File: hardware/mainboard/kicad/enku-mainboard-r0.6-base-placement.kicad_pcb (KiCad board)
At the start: 4 copper layers, 59 x 101 mm, 120 parts, among them J1 1S LiPo + NTC, J2 Hirose DM3AT-SF-PEJM5, J3 FH34SRJ-24S-0.5SH(50), J5 GCT USB4105-GF-A-120, J6 4-pin pogo dock, J7 Tag-Connect TC2030-IDC-NL, Q1 IRLML6346TRPBF, SW1 HARD POWER, SW2 BOOT / RECOVERY, SW3 BTN_L1, SW4 BTN_L2, SW5 BTN_R1, SW6 BTN_R2, U1 ESP32-S3-WROOM-1-N16R8, U2 TPS2121, U3 BQ25185DLHR, U4 TPS63802DLAR, U5 BMI270, U8 USBLC6-2SC6

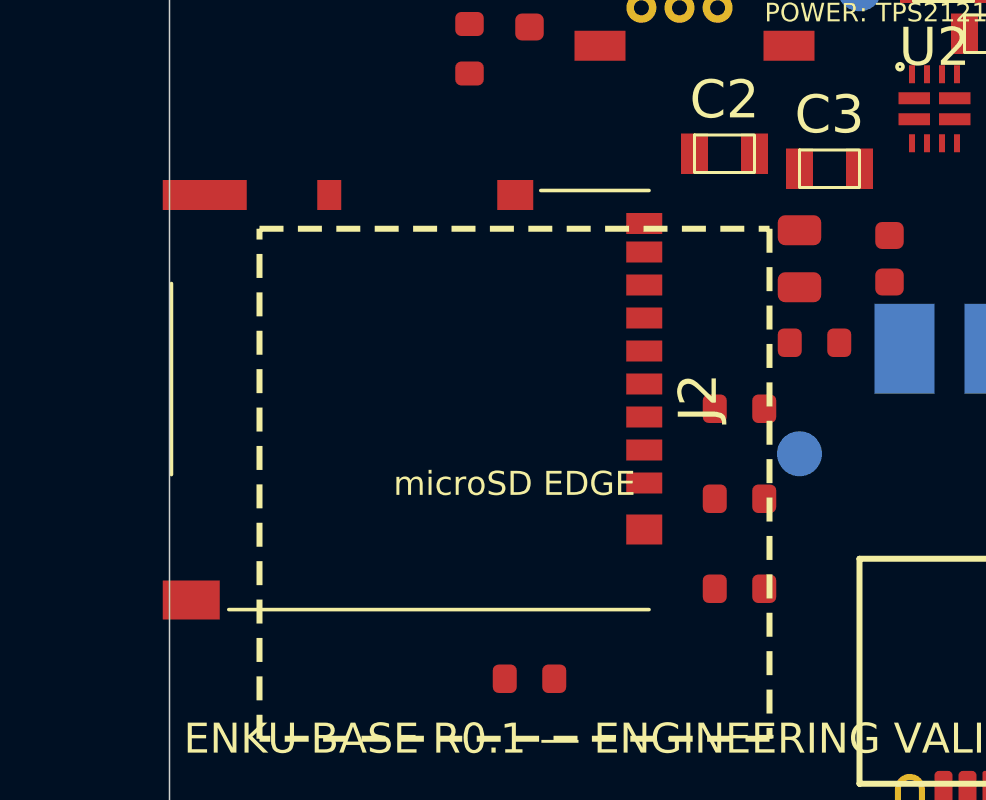
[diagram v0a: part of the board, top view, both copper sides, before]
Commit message: Correct Hirose J2 copper edge clearance by inward placement
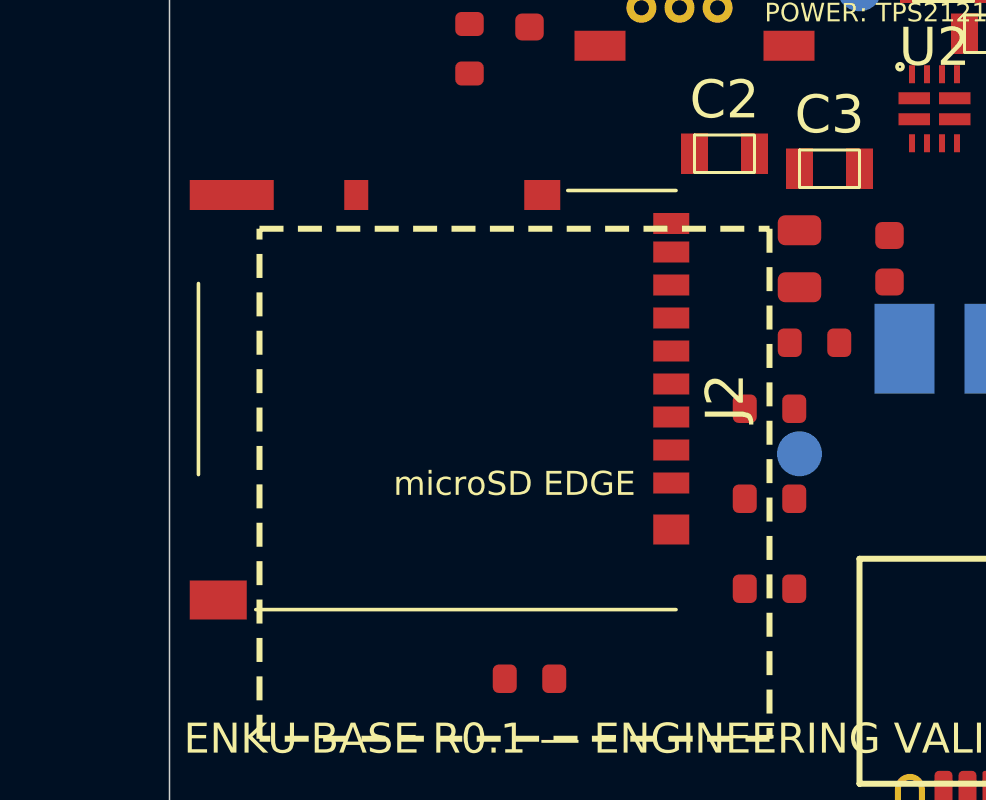
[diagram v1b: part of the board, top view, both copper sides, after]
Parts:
- moved R19 1.00 mm to (38.0, 101.0)
- moved R20 1.00 mm to (38.0, 104.0)
- moved R21 1.00 mm to (38.0, 107.0)
- moved J2 0.90 mm to (27.0, 100.7)
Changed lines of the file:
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@@
   )
   (footprint "ENKU:MICROSD_DM3AT_ENKU" (layer "F.Cu")
-    (at 26.1 100.7 270)
+    (at 27 100.7 270)
     (property "Reference" "J2" (at -0.075 -9.525 90) (layer "F.SilkS"))
     (property "Value" "Hirose DM3AT-SF-PEJM5" (at -0.075 9.575 90) (layer "F.Fab") hide)
@@
   )
   (footprint "Resistor_SMD:R_0603_1608Metric" (layer "F.Cu")
-    (at 37 101)
+    (at 38 101)
     (property "Reference" "R19" (at 0 -1.5 0) (layer "F.SilkS") hide)
     (property "Value" "0R" (at 0 1.5 0) (layer "F.Fab") hide)
@@
   )
   (footprint "Resistor_SMD:R_0603_1608Metric" (layer "F.Cu")
-    (at 37 107)
+    (at 38 107)
     (property "Reference" "R21" (at 0 -1.5 0) (layer "F.SilkS") hide)
     (property "Value" "0R (22R tune)" (at 0 1.5 0) (layer "F.Fab") hide)
@@
   )
   (footprint "Resistor_SMD:R_0603_1608Metric" (layer "F.Cu")
-    (at 37 104)
+    (at 38 104)
     (property "Reference" "R20" (at 0 -1.5 0) (layer "F.SilkS") hide)
     (property "Value" "0R (22R tune)" (at 0 1.5 0) (layer "F.Fab") hide)

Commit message: layout: move legacy study annotations off Base fabrication silkscreen and remove frontlight ghost zone
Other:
- board text removed: "FL REMAP 0R / DNP"
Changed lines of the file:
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@@
     (stroke (width 0.05) (type default)) (fill none) (layer "Edge.Cuts"))
   (gr_text "ENKU MAINBOARD R0.1 — PORTRAIT PCB SHELL"
-    (at 47 22.5) (layer "F.SilkS")
+    (at 47 22.5) (layer "Dwgs.User")
     (effects (font (size 1.2 1.2) (thickness 0.2))))
   (gr_text "ENKU BASE R0.1 — ENGINEERING VALIDATION"
-    (at 34.5 112.0) (layer "F.SilkS")
+    (at 34.5 112.0) (layer "Dwgs.User")
     (effects (font (size 1 1) (thickness 0.18))))
   (gr_rect (start 20.5 21) (end 26.25 69)
-    (stroke (width 0.2) (type dash)) (fill none) (layer "F.SilkS"))
+    (stroke (width 0.2) (type dash)) (fill none) (layer "Dwgs.User"))
   (gr_text "ESP32 ANTENNA KEEP-OUT"
-    (at 21.6 46.5 90) (layer "F.SilkS")
+    (at 21.6 46.5 90) (layer "Dwgs.User")
     (effects (font (size 0.8 0.8) (thickness 0.12))))
   (gr_rect (start 45 24) (end 72 39)
-    (stroke (width 0.2) (type dash)) (fill none) (layer "F.SilkS"))
+    (stroke (width 0.2) (type dash)) (fill none) (layer "Dwgs.User"))
   (gr_text "EPD HV / FPC ZONE"
-    (at 58.5 31.5) (layer "F.SilkS")
+    (at 58.5 31.5) (layer "Dwgs.User")
     (effects (font (size 0.9 0.9) (thickness 0.14))))
   (gr_rect (start 69 48) (end 73.5 82)
-    (stroke (width 0.2) (type default)) (fill none) (layer "F.SilkS"))
+    (stroke (width 0.2) (type default)) (fill none) (layer "Dwgs.User"))
   (gr_text "BUTTON RAIL"
-    (at 71.2 65 90) (layer "F.SilkS")
+    (at 71.2 65 90) (layer "Dwgs.User")
     (effects (font (size 0.8 0.8) (thickness 0.12))))
   (gr_rect (start 21 95) (end 38 112)
-    (stroke (width 0.2) (type dash)) (fill none) (layer "F.SilkS"))
+    (stroke (width 0.2) (type dash)) (fill none) (layer "Dwgs.User"))
   (gr_text "microSD EDGE"
-    (at 29.5 103.5) (layer "F.SilkS")
+    (at 29.5 103.5) (layer "Dwgs.User")
     (effects (font (size 0.8 0.8) (thickness 0.12))))
   (gr_rect (start 41 106) (end 53 113.5)
-    (stroke (width 0.2) (type default)) (fill none) (layer "F.SilkS"))
+    (stroke (width 0.2) (type default)) (fill none) (layer "Dwgs.User"))
   (gr_text "USB-C"
-    (at 47 109.7) (layer "F.SilkS")
+    (at 47 109.7) (layer "Dwgs.User")
     (effects (font (size 0.8 0.8) (thickness 0.12))))
   (gr_rect (start 38 96) (end 56 102)
@@
     (effects (font (size 0.8 0.8) (thickness 0.12)) (justify mirror)))
   (gr_rect (start 23 25) (end 38 33)
-    (stroke (width 0.2) (type default)) (fill none) (layer "F.SilkS"))
+    (stroke (width 0.2) (type default)) (fill none) (layer "Dwgs.User"))
   (gr_text "HARD POWER"
-    (at 30.5 29) (layer "F.SilkS")
+    (at 30.5 29) (layer "Dwgs.User")
     (effects (font (size 0.8 0.8) (thickness 0.12))))
   (gr_text "54.0 mm"
@@
     (pad "" np_thru_hole circle (at 0 0) (size 2.2 2.2) (drill 2.2) (layers "*.Cu" "*.Mask")))
   (gr_text "ENKU BASE R0.1 — ENGINEERING PROTOTYPE"
-    (at 47 24.5) (layer "F.SilkS")
+    (at 47 24.5) (layer "Dwgs.User")
     (effects (font (size 0.75 0.75) (thickness 0.12))))
   (footprint "ENKU:FH34SRJ-24S-0.5SH" (layer "F.Cu")
@@
     (pad "3" smd rect (at 1.0 0) (size 1.0 0.8) (layers "F.Cu" "F.Paste" "F.Mask") (net 30 "EPD_SW"))
   )
-  (gr_rect (start 63.5 36.5) (end 72 45)
-    (stroke (width 0.15) (type dash)) (fill none) (layer "F.SilkS"))
-  (gr_text "FL REMAP 0R / DNP"
-    (at 67.8 43.8) (layer "F.SilkS")
-    (effects (font (size 0.65 0.65) (thickness 0.1))))
   (footprint "RF_Module:ESP32-S3-WROOM-1" (layer "F.Cu")
     (at 33 45 90)
@@
     (pad "2" smd rect (at 1 0 90) (size 0.9 1.35) (layers "F.Cu" "F.Paste" "F.Mask") (net 1 "GND"))
   )
-  (gr_text "POWER: TPS2121 / BQ25185 / TPS63802" (at 46.5 87.8) (layer "F.SilkS")
+  (gr_text "POWER: TPS2121 / BQ25185 / TPS63802" (at 46.5 87.8) (layer "Dwgs.User")
     (effects (font (size 0.62 0.62) (thickness 0.11))))
-  (gr_text "IMU QUIET ZONE" (at 31.5 76.8) (layer "F.SilkS")
+  (gr_text "IMU QUIET ZONE" (at 31.5 76.8) (layer "Dwgs.User")
     (effects (font (size 0.55 0.55) (thickness 0.11))))
   (gr_text "OPEN HARDWARE — VERIFY DRC/ERC BEFORE FAB" (at 47 112.4) (layer "B.SilkS")
